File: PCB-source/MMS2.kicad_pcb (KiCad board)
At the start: 4 copper layers, 90 x 50 mm, 194 parts, among them J1 86093488324755V1LF, J2 AMASS XT60, J3 Programming header, J4 Conn_01x16_Socket, J5 Conn_01x03_Pin, J7 AMASS XT60, J8 RJ45_LED_Shielded, J800 USB_C_Receptacle_USB2.0_16P, J9 RJ45_LED_Shielded, Q2 AO3400A, Q3 AO3400A, Q5 AO3400A, Q6 AO3400A, Q7 AO3400A, Q700 MMST3904, SW1 BOOT, SW2 RESET, U1 STM32F405RGTx, U2 LMR36520ADDAR, U3 TPD2EUSB30DRTR-TP, U301 TPS563200, U302 CH334P, U4 TPD2EUSB30DRTR-TP, U401 TPD2EUSB30DRTR-TP, U5 LM74700, U500 TJA1044GTK_3Z, U501 TJA1044GTK_3Z, U6 AT24C256C, U7 CH32V003FxUx, U700 STM32F103CBTx, U801 FSUSB42UMX, X1 X32258MOB4SI, X2 Q13FC1350000400, Y700 Crystal_GND24, Y900 Crystal_GND24

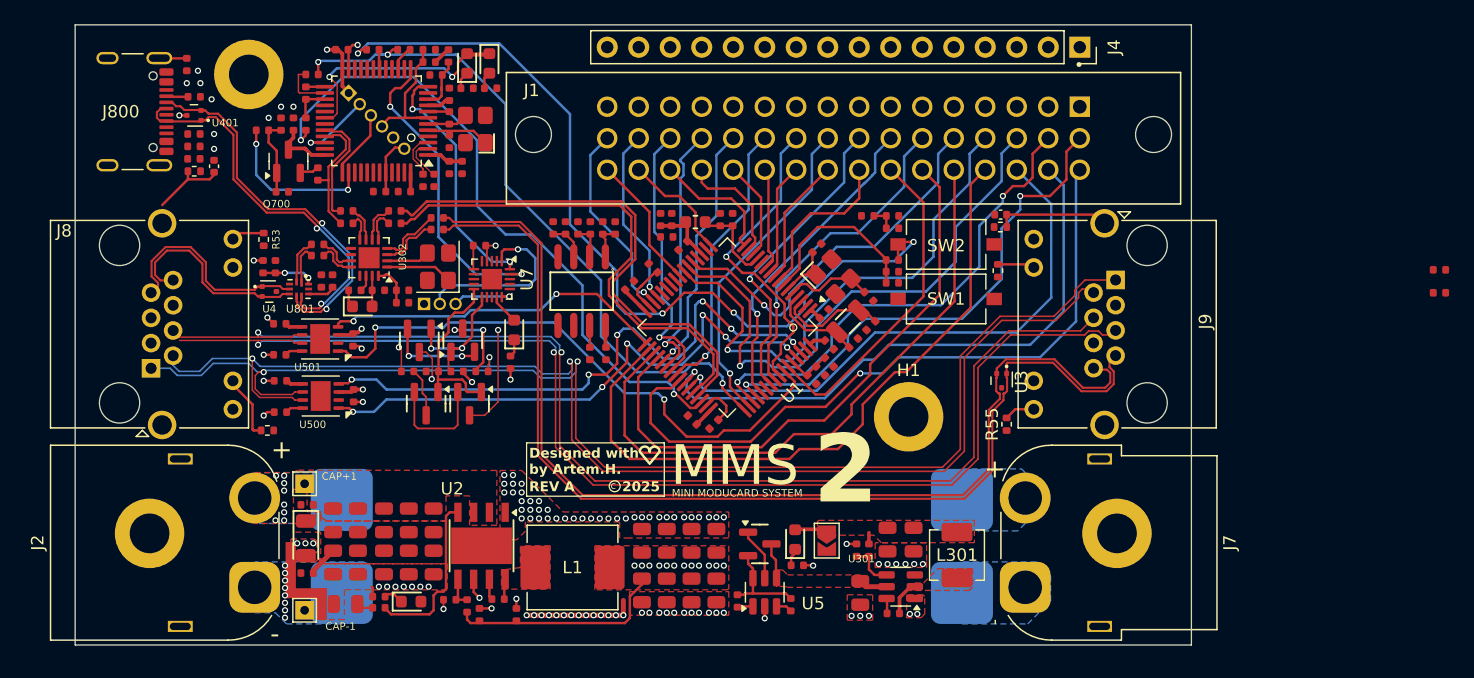
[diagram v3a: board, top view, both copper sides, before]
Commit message: silk job, signal ratnest done
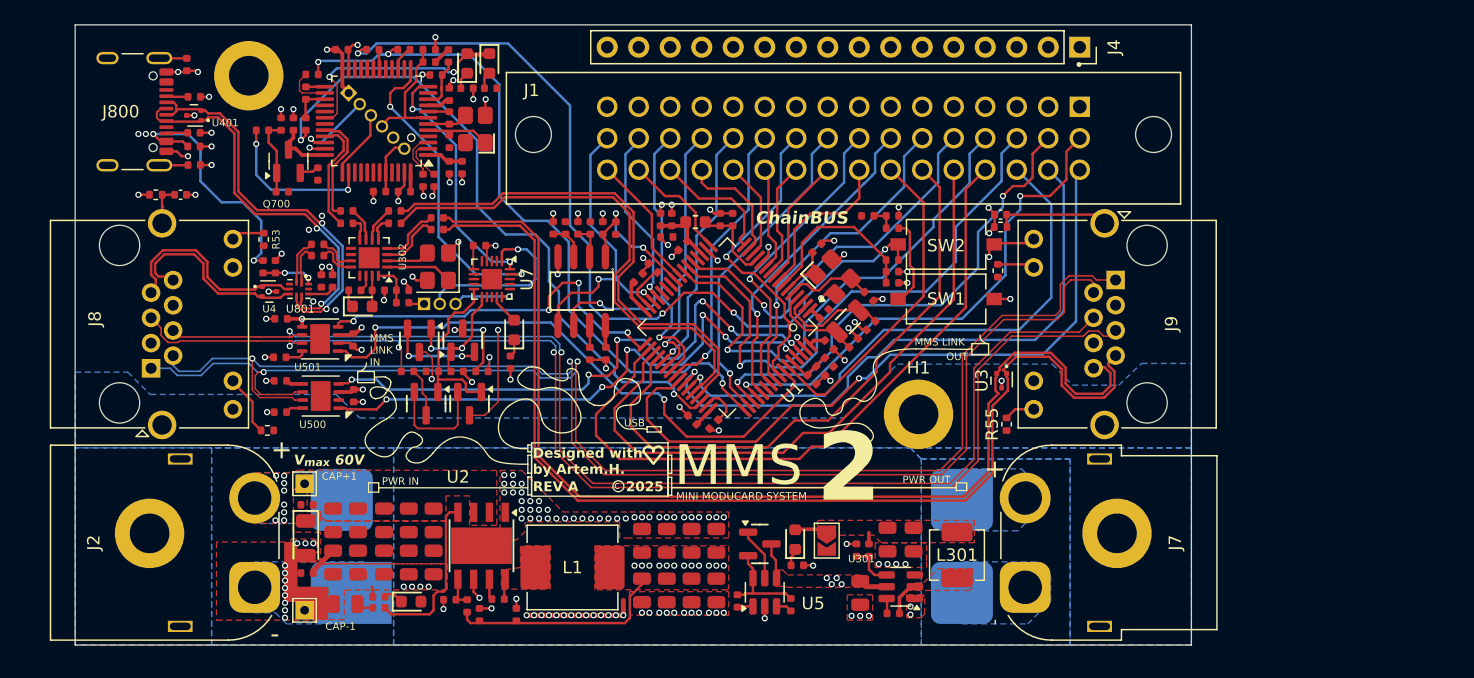
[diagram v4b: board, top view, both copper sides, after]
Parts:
- removed R23, R407: 220Ω, PCM_JLCPCB:R_0402
- added NT2: custom net tie, PgndNetTie:SHLD, B.Cu at (104.5, 131.3)
- added REF**: WEEE-Logo_4.2x6mm_SilkScreen, Symbol:WEEE-Logo_4.2x6mm_SilkScreen, B.Cu at (111.9, 98.0)
- moved R51 3.64 mm to (86.5, 101.7), turned to 180 degrees
- moved C45 3.55 mm to (88.5, 101.7), turned to 0 degrees
- moved C402 0.92 mm to (125.4, 108.4)
- moved H1 0.82 mm to (148.0, 119.4)
- moved R805 0.50 mm to (89.6, 99.3)
- moved C503 0.41 mm to (96.6, 111.7)
- moved R501 0.20 mm to (96.5, 114.8)
- moved NT1 0.13 mm to (100.0, 135.7)
- moved H4 0.10 mm to (94.0, 92.1)
- moved R800 0.10 mm to (89.6, 96.7)
- moved R21 0.07 mm to (123.6, 104.4), turned to 90 degrees
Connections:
- R21 pad 2: /QSPI_FLASH/A0 -> /MCU/I2C_Memory_addr
- R22 pad 1: /QSPI_FLASH/A0 -> /MCU/I2C_Memory_addr
- U1 pad 25: unconnected-(U1-PC5-Pad25) -> /MCU/I2C_Memory_addr
- U6 pad 1: /QSPI_FLASH/A0 -> /MCU/I2C_Memory_addr
- U6 pad 5: /MCU/I2C_Memory.SDA -> /Interboard_connector/Chainbus.SDA
- U6 pad 6: /MCU/I2C_Memory.SCL -> /Interboard_connector/Chainbus.SCL
- U7 pad 12: (no net) -> unconnected-(U7-PC5-Pad12)
- U7 pad 13: (no net) -> unconnected-(U7-PC6-Pad13)
- U7 pad 16: (no net) -> unconnected-(U7-PD2-Pad16)
- U7 pad 17: (no net) -> unconnected-(U7-PD3-Pad17)
- U7 pad 18: (no net) -> unconnected-(U7-PD4-Pad18)
- U7 pad 2: (no net) -> unconnected-(U7-PA1-Pad2)
- U7 pad 3: (no net) -> unconnected-(U7-PA2-Pad3)
- U7 pad 5: (no net) -> unconnected-(U7-PD0-Pad5)
- U7 pad 7: (no net) -> unconnected-(U7-PC0-Pad7)
- U7 pad 8: (no net) -> unconnected-(U7-PC1-Pad8)
- U7 pad 9: (no net) -> unconnected-(U7-PC2-Pad9)
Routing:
- net GND: track 28.8 -> 99.0 mm, vias 110 -> 164
- net VBUS: track 5.99 -> 25.9 mm, vias 1 -> 8
- net /CAN auto terminator/CAN1.-: track 123.9 -> 105.1 mm
- net /CAN auto terminator/CAN1.+: track 118.6 -> 103.1 mm
- net /MCU/I2C_Memory_addr: track 0.00 -> 11.9 mm, vias 0 -> 2
- net /Interboard_connector/Chainbus.SCL: track 14.5 -> 24.8 mm, vias 1 -> 2
- net /Interboard_connector/Chainbus.SDA: track 16.6 -> 24.6 mm, vias 1 -> 2
- net /MCU/USR_BUTTON: track 0.00 -> 7.22 mm
- net /QSPI_FLASH/A0: track 2.92 -> 0.00 mm
- net /CAN_TR2/CAN.RX: track 27.9 -> 30.7 mm, vias 2 -> 4
- net Net-(C45-Pad1): track 6.06 -> 3.49 mm
- net /MMS_CONNECTOR_DOWNSTREAM/USB_MMS_CONN.D-: track 86.1 -> 88.6 mm
- net /CAN auto terminator/CAN2.+: track 104.2 -> 106.6 mm
- net Net-(J800-SHIELD): track 2.22 -> 4.55 mm
- net /MMS_CONNECTOR_DOWNSTREAM/USB_MMS_CONN.D+: track 85.6 -> 87.7 mm
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- added copper zone on F.Cu, net GNDPWR
- added copper zone on B.Cu, net SHLD
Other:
- board text added: "Autorowi pewnie chodziło o to, żeby przerobić standardowe złącza programatora/debuggera (np. 2.54 mm goldpiny) na te nowsze, gęstsze 1.27 mm raster - bo w ARM-owym świecie od dawna stosuje się złącze SWD/JTAG w tym kroku."
- board text added: "ChainBUS"
- board text added: "FW VER. MC1"
- board text added: "FW VER. MC2"
- board text added: "MMS LINK IN"
- board text added: "OUT"
- board text added: "PWR IN"
- board text added: "PWR OUT"
- board text added: "QC"
- board text added: "SN"
- board text added: "V_{max} 60V"
- board text added: "przerobić konektory na tych ... o jezu ... oh ... na ten nowy cuś.... na te 1.27. milimetra ... he he do SWD"

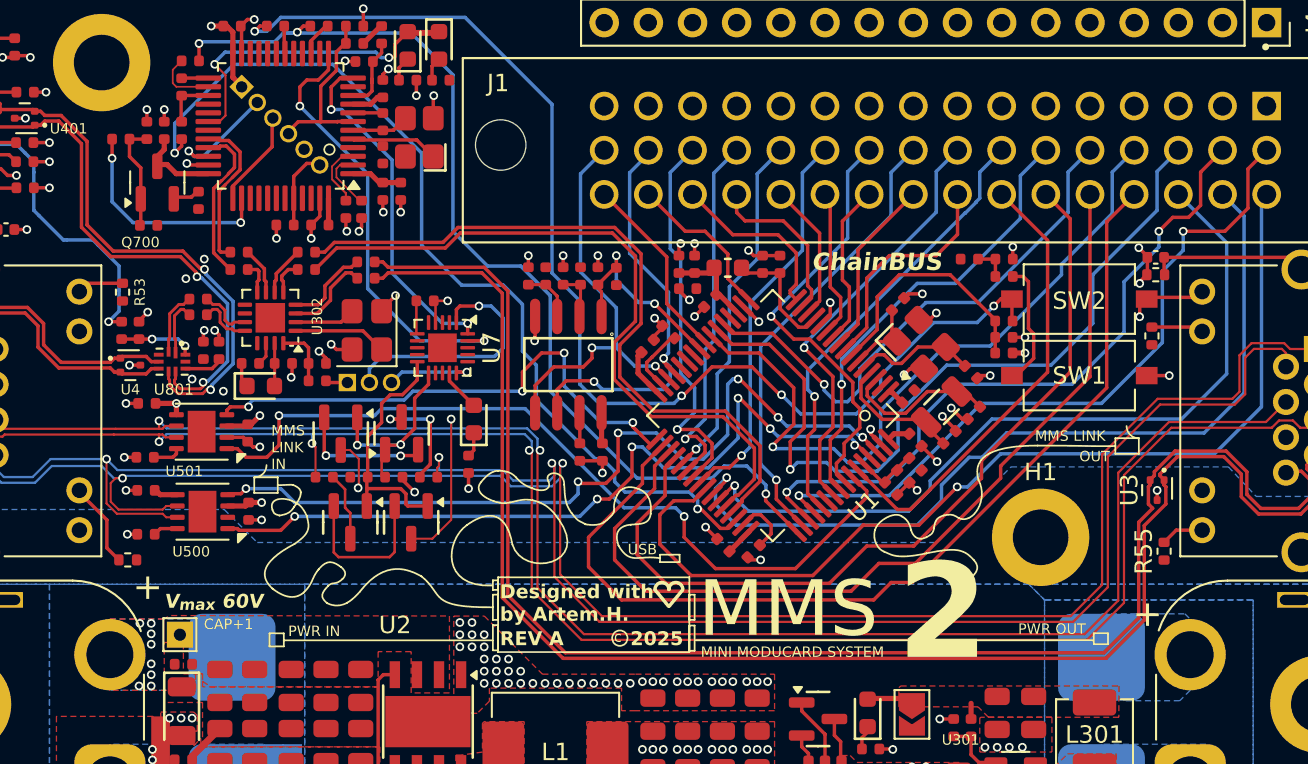
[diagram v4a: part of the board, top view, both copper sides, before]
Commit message: change can term add usr led
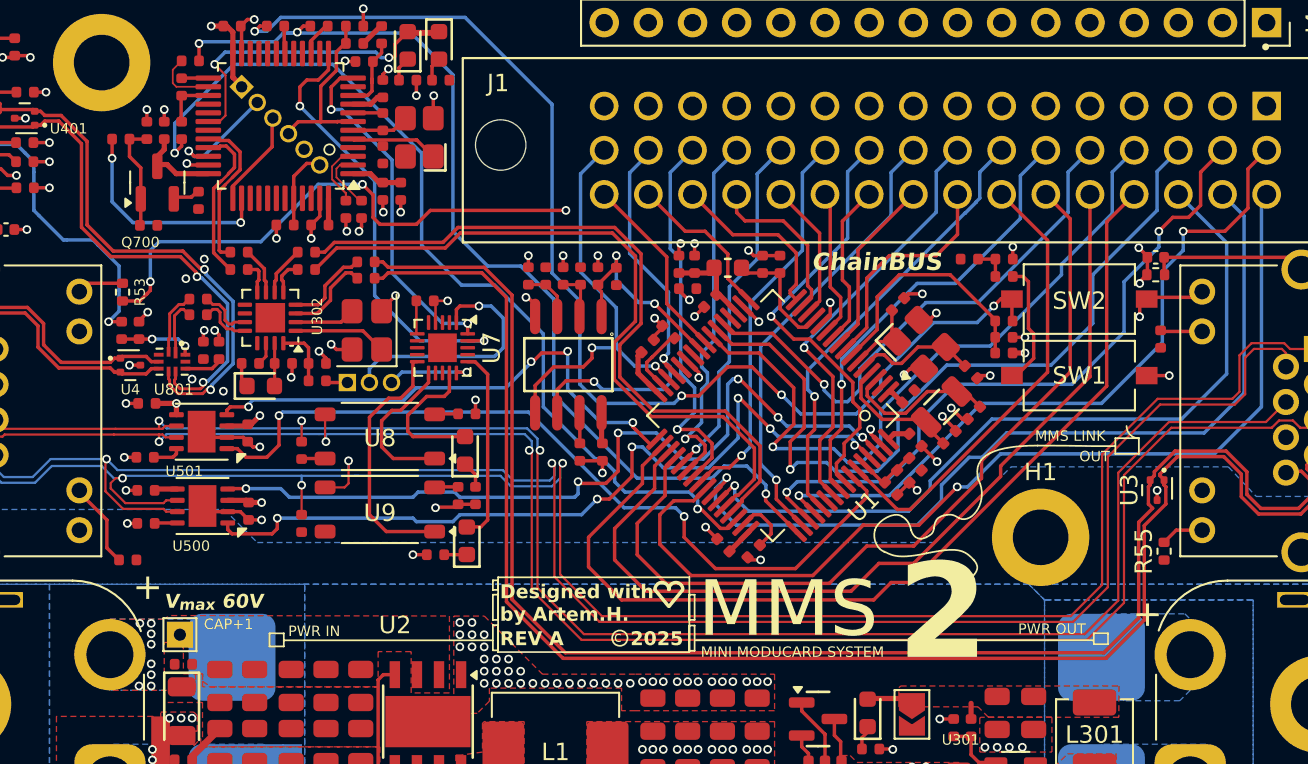
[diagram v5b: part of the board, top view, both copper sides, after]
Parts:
- removed Q2, Q3, Q5, Q6: AO3400A, PCM_JLCPCB:Q_SOT-23
- removed R52, R54: 1k, Resistor_SMD:R_0402_1005Metric
- removed REF**: WEEE-Logo_4.2x6mm_SilkScreen, Symbol:WEEE-Logo_4.2x6mm_SilkScreen
- added D3: Red, PCM_JLCPCB:D_0603, F.Cu at (115.0, 119.6)
- added R23: 220Ω, PCM_JLCPCB:R_0402, F.Cu at (113.2, 120.4)
- added R25: 220Ω, PCM_JLCPCB:R_0402, F.Cu at (154.9, 108.0)
- added R26: 220Ω, PCM_JLCPCB:R_0402, F.Cu at (95.5, 120.7)
- added U8: TLP175A, Package_SO:Toshiba_SOIC-4-6_4.4x3.6mm_P1.27mm, F.Cu at (110.0, 113.6)
- added U9: TLP175A, Package_SO:Toshiba_SOIC-4-6_4.4x3.6mm_P1.27mm, F.Cu at (110.0, 117.8)
- R3, R5: value 10kΩ -> 1kΩ
- moved R1 7.77 mm to (105.5, 118.6), turned to -90 degrees
- moved R3 7.19 mm to (115.0, 112.3), turned to 0 degrees
- moved R5 3.85 mm to (114.5, 117.0), turned to -90 degrees
- moved R2 2.02 mm to (105.5, 114.4), turned to -90 degrees
- moved D4 1.87 mm to (114.9, 114.4)
- moved R24 1.84 mm to (115.5, 117.0)
- moved R500 0.62 mm to (96.5, 118.6)
- moved U500 0.33 mm to (99.8, 117.6)
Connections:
- net /CH32V003/LED renamed /CH32V003/LED1
- R1 pad 1: /CAN auto terminator/CAN2.+ -> /CAN auto terminator/CAN2.-
- R2 pad 1: /CAN auto terminator/CAN1.+ -> /CAN auto terminator/CAN1.-
- R3 pad 1: /CAN auto terminator/CAN_AUTOTERM.1 -> Net-(R3-Pad1)
- R5 pad 1: /CAN auto terminator/CAN_AUTOTERM.2 -> Net-(R5-Pad1)
- R53 pad 1: /MMS_CONNECTOR_UPSTREAM/TXD2_LED -> /MCU/USER_LED_1
- R55 pad 1: /MMS_CONNECTOR_DOWNSTREAM/TXD2_LED -> /MCU/USER_LED_2
- U7 pad 10: /CAN auto terminator/CAN_AUTOTERM.1 -> /CAN auto terminator/CAN_AUTOTERM.2
- U7 pad 11: /CAN auto terminator/CAN_AUTOTERM.2 -> /CAN auto terminator/CAN_AUTOTERM.1
- U7 pad 16: unconnected-(U7-PD2-Pad16) -> /CH32V003/LED2
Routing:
- net /MCU/USER_LED_1: track 0.00 -> 31.7 mm, vias 0 -> 3
- net /CH32V003/LED2: track 0.00 -> 11.2 mm
- net Net-(Q5-S): track 9.05 -> 0.00 mm
- net Net-(Q2-S): track 7.90 -> 0.00 mm, vias 2 -> 0
- net /CAN auto terminator/CAN1.-: track 105.1 -> 97.6 mm
- net GND: track 99.0 -> 105.5 mm, vias 164 -> 165
- net Net-(R1-Pad2): track 6.36 -> 0.00 mm, vias 2 -> 0
- net /CH32V003/LED1: track 2.44 -> 8.36 mm
- net /CAN auto terminator/CAN_AUTOTERM.1: track 14.2 -> 8.99 mm
- net /CAN auto terminator/CAN_AUTOTERM.2: track 11.6 -> 14.6 mm, vias 2 -> 0
- net Net-(R2-Pad2): track 3.95 -> 1.36 mm
- net /CAN auto terminator/CAN2.-: track 110.1 -> 108.0 mm
- net Net-(R5-Pad1): track 0.00 -> 1.36 mm
- net Net-(R3-Pad1): track 0.00 -> 1.36 mm
- net Net-(D3-Pad1): track 0.00 -> 1.30 mm
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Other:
- board text removed: "MMS LINK IN"

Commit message: DRC PASS, preparing bom for production
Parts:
- removed D402: Red, PCM_JLCPCB:D_0603
- removed the H4 at (164.0, 129.0)
- removed the H4 at (94.0, 92.1)
- removed R6: 100kΩ, PCM_JLCPCB:R_0402
- added D6: SS34, PCM_JLCPCB:D_SMA, F.Cu at (90.4, 99.8)
- added H2: M3 mount, MountingHole:MountingHole_3.2mm_M3_DIN965_Pad, F.Cu at (94.0, 92.1)
- added H3: M3 mount, MountingHole:MountingHole_3.2mm_M3_DIN965_Pad, F.Cu at (164.0, 129.0)
- R12: value 1.2kΩ -> 100kΩ; footprint PCM_JLCPCB:R_0402 -> PCM_JLCPCB:R_0603
- moved C45 20.4 mm to (95.5, 120.9)
- moved R51 20.2 mm to (95.5, 119.8), turned to 0 degrees
- moved C800 7.90 mm to (82.6, 101.5)
- moved R12 7.34 mm to (111.7, 135.5)
- moved R800 6.91 mm to (84.6, 101.5)
- moved C16 5.81 mm to (107.6, 135.0)
- moved R501 3.96 mm to (100.4, 115.5), turned to 0 degrees
- moved R805 3.18 mm to (87.3, 101.5), turned to 180 degrees
- moved R500 2.41 mm to (98.6, 119.9), turned to 0 degrees
- moved C501 2.21 mm to (98.4, 115.5), turned to 0 degrees
- moved R26 2.06 mm to (97.1, 119.4), turned to -90 degrees
- moved C27 1.01 mm to (113.6, 135.7)
- moved R10 0.82 mm to (105.3, 135.1), turned to -90 degrees
- moved C26 0.71 mm to (132.2, 120.1), turned to -45 degrees
- moved C801 0.47 mm to (89.2, 91.6)
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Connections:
- C19 pad 1: VBUS -> +5V
- JP301 pad 2: /VRM/TPS563201/VOUT -> +3V3
- Q7 pad 3: VBUS -> +5V
- R12 pad 1: Net-(D402-Pad1) -> /VRM/LMR36520ADDAR/LMR36520ADDAR_VOUT
- R12 pad 2: GND -> /VRM/LMR36520ADDAR/FB
- R25 pad 2: +3V3 -> /MCU/USER_LED_2
- R55 pad 1: /MCU/USER_LED_2 -> +3V3
- U1 pad 26: /MCU/USER_LED_1 -> /MCU/USER_LED_2
- U1 pad 27: /MCU/USER_LED_2 -> /MCU/USER_LED_1
- U1 pad 54: unconnected-(U1-PD2-Pad54) -> /MCU/USR_BUTTON
- U301 pad 3: VBUS -> +5V
- U301 pad 5: VBUS -> +5V
- U5 pad 4: VBUS -> +5V
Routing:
- net +12V: track 0.00 -> 119.4 mm
- net +3V3: track 37.2 -> 105.1 mm, vias 3 -> 27
- net /MCU/USER_LED_2: track 1.21 -> 37.2 mm, vias 1 -> 2
- net /MCU/USER_LED_1: track 31.7 -> 51.2 mm, vias 3 -> 4
- net +5V: track 6.63 -> 25.0 mm, vias 2 -> 19
- net /MCU/USR_BUTTON: track 7.22 -> 22.8 mm, vias 0 -> 2
- net VBUS: track 25.9 -> 40.0 mm, vias 8 -> 7
- net GND: track 105.5 -> 118.8 mm, vias 165 -> 187
- net /VRM/LMR36520ADDAR/VCC: track 3.06 -> 12.1 mm, vias 1 -> 0
- net Net-(J800-SHIELD): track 4.55 -> 13.3 mm
- net /USBC_CONN/CC2: track 1.74 -> 7.74 mm, vias 0 -> 2
- net Net-(C45-Pad1): track 3.49 -> 9.34 mm
- net /CAN auto terminator/CAN2.-: track 108.0 -> 110.4 mm
- net /CAN auto terminator/CAN2.+: track 107.5 -> 109.2 mm
- net Net-(D402-Pad1): track 1.64 -> 0.00 mm
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- added copper zone on F.Cu, net +3V3
- added copper zone on In2.Cu, net +3V3
- added copper zone on F.Cu, net +5V
- added copper zone on In2.Cu, net +5V
- added copper zone on In2.Cu, net BRD_VIN
- added copper zone on In2.Cu, net GND
- added copper zone on B.Cu, net VBUS
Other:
- board text added: "CAN1"
- board text added: "CAN2"
- board text added: "RST"
- board text added: "USR"
